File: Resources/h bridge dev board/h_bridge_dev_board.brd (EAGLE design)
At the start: 160 x 100 mm, 99 parts, among them IC1 74LS08N, IC2 74LS08N, IC3 74LS08N, IC4 7404N, IC5 74LS595N, IC6 74158N, IC7 LM358N, J1 J50MM, J2 J50MM, J25 J50MM, J26 J50MM, J27 J50MM, J28 J50MM, J3 J50MM, J4 J50MM

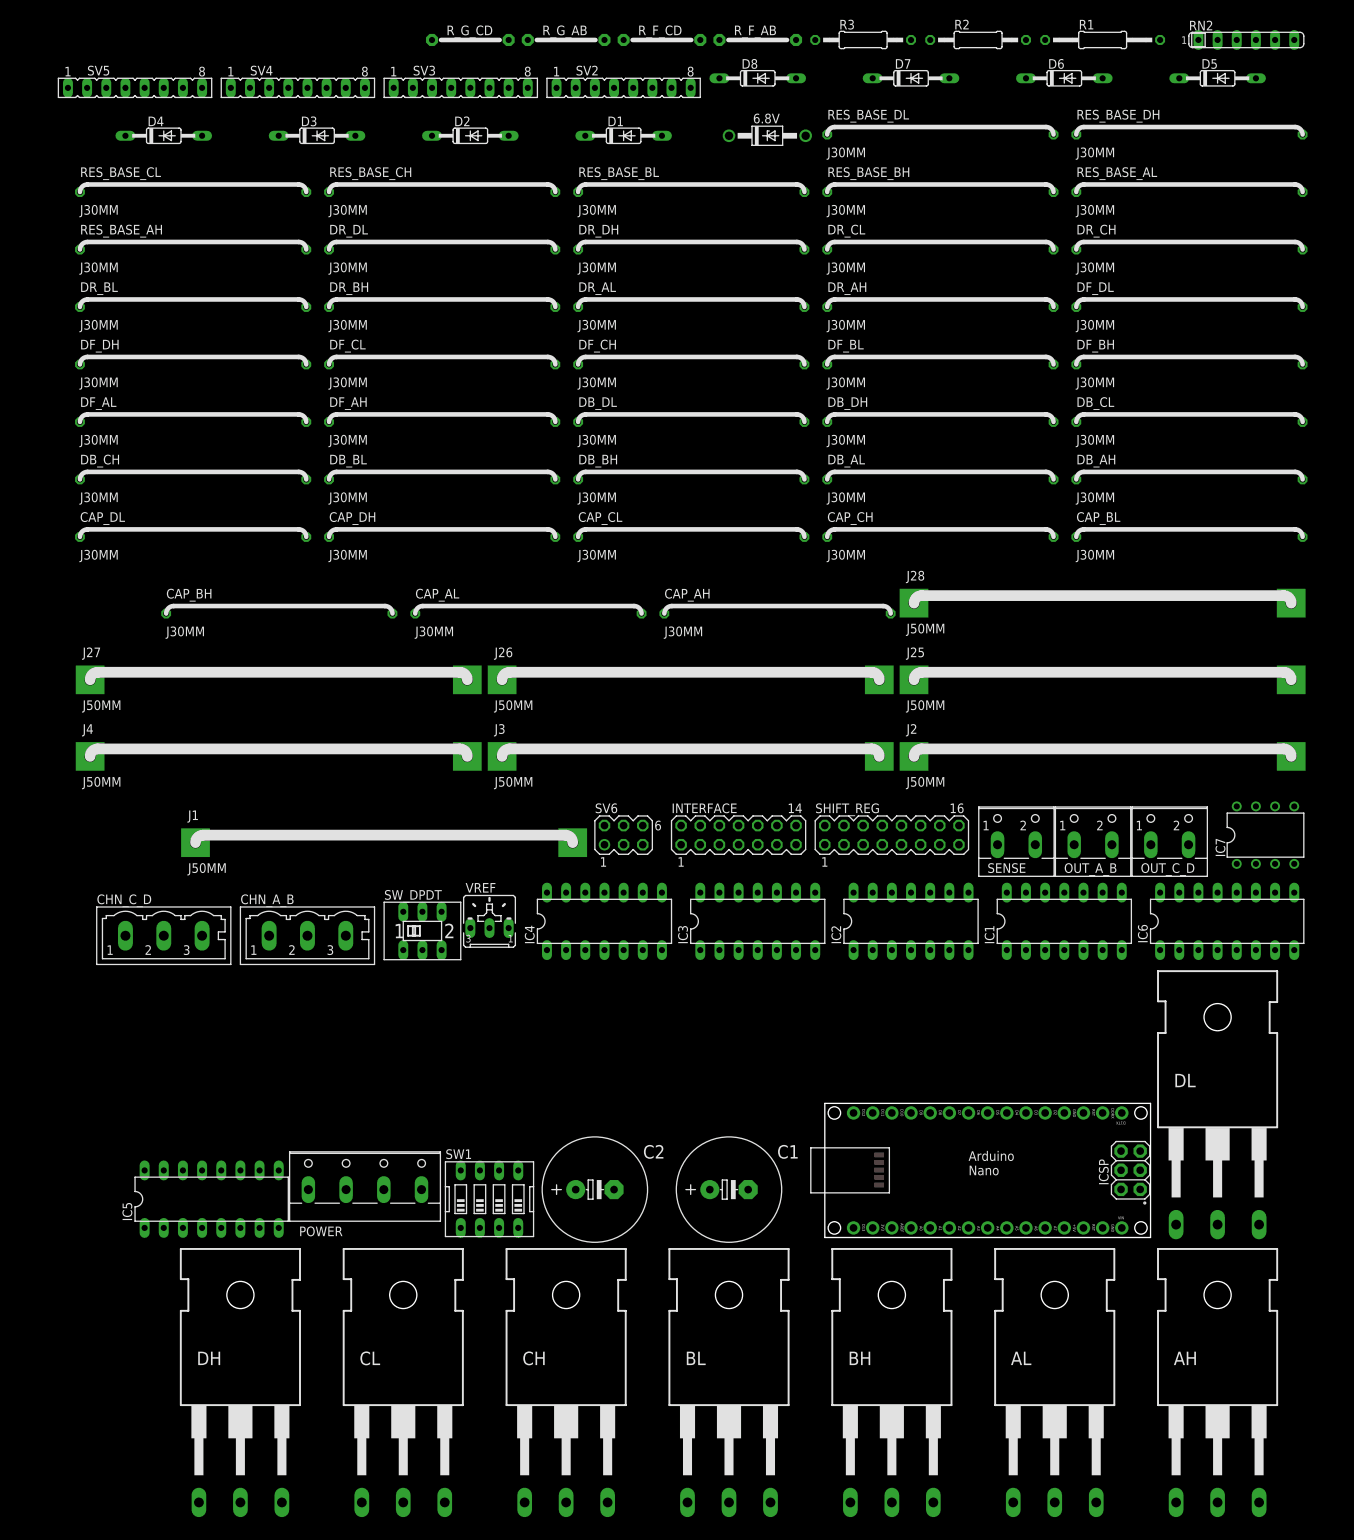
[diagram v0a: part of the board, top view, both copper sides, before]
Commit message: added opto coupler in schematic
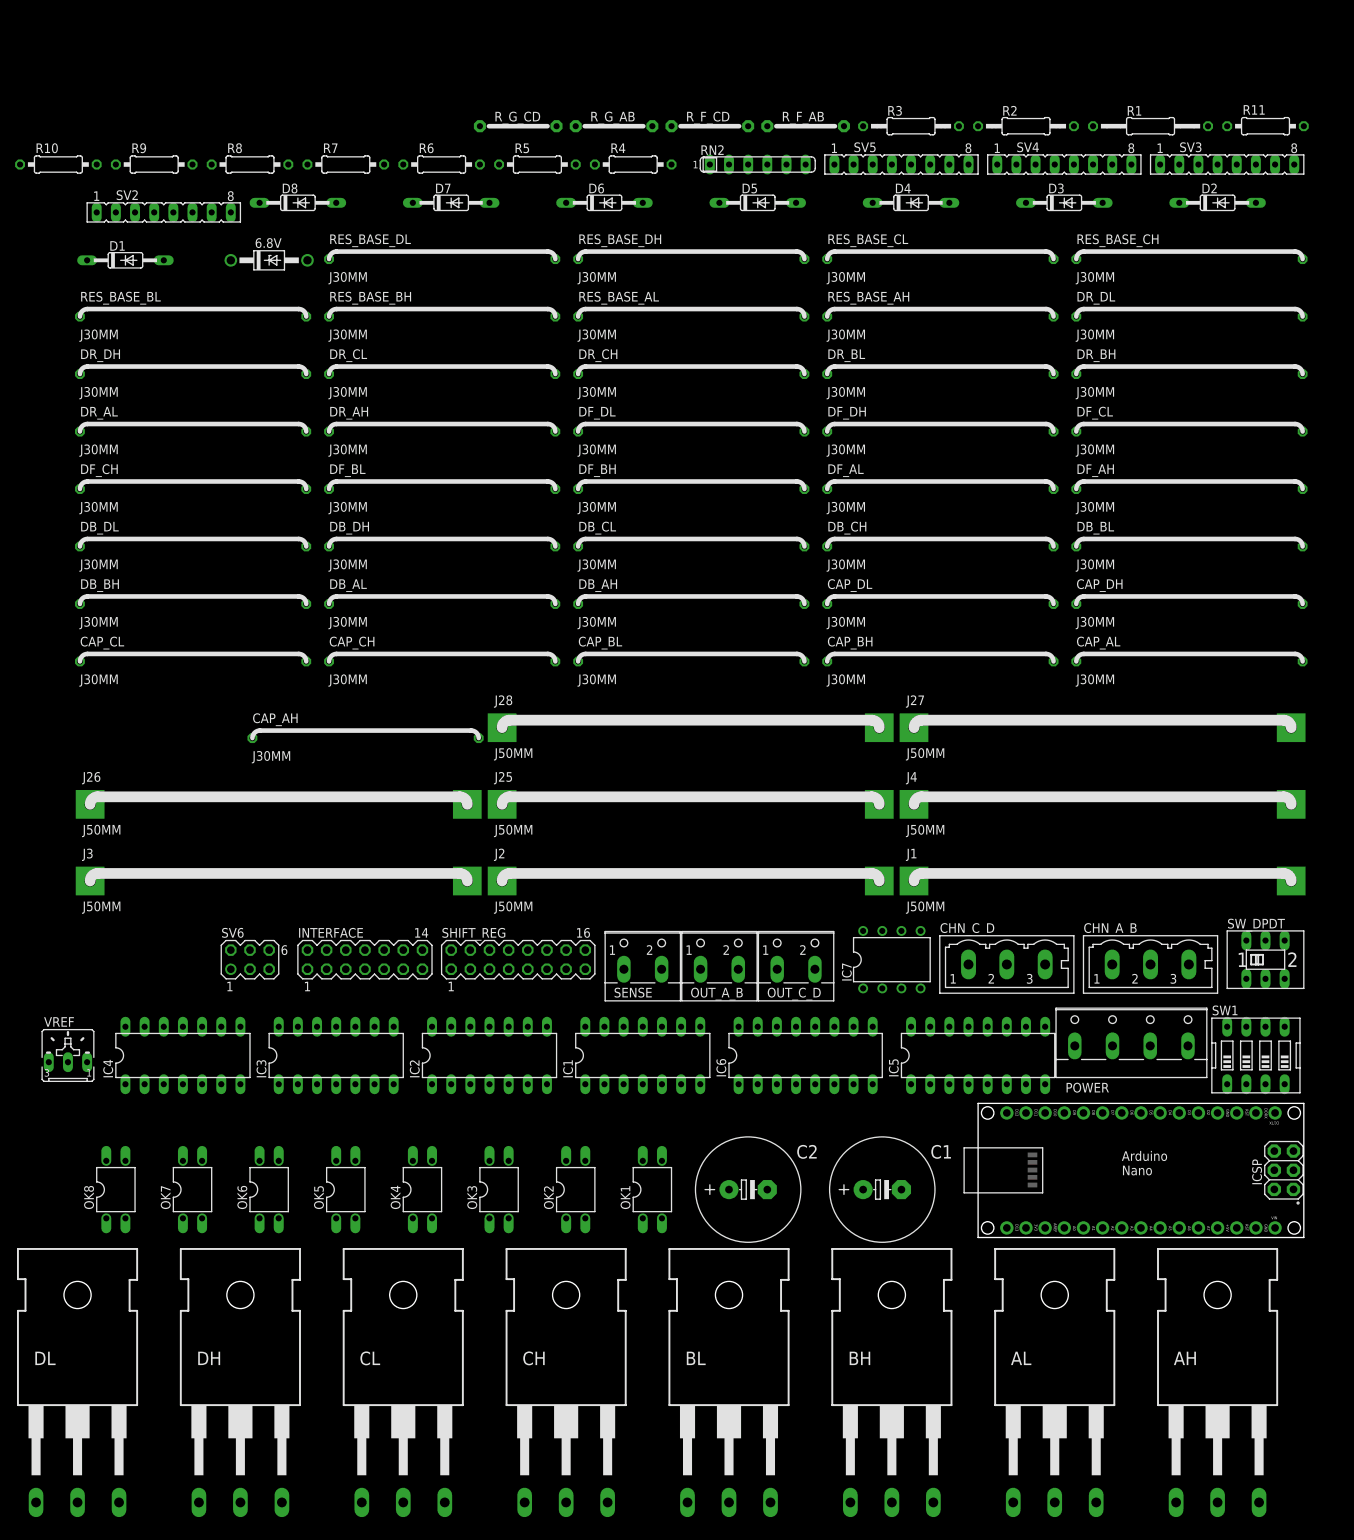
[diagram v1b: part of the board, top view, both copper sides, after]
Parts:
- added OK1, OK2, OK3, OK4, OK5, OK6, OK7, OK8: PC817, optocoupler:DIL04
- added R10, R11, R4, R5, R6, R7, R8, R9: 220, resistor:0207/10
- R2: value 3k -> 3.3k
- moved DL 155.6 mm to (-176.5, 30.5)
- moved CHN_A_B 111.8 mm to (-34.3, 74.9)
- moved SW_DPDT 111.8 mm to (-19.1, 74.9)
- moved CHN_C_D 111.8 mm to (-53.3, 74.9)
- moved J27 109.4 mm to (-40.6, 106.7)
- moved J4 109.4 mm to (-40.6, 96.5)
- moved POWER 103.4 mm to (-36.8, 64.8)
- moved IC5 103.4 mm to (-57.1, 62.2)
- moved SW1 103.4 mm to (-20.3, 62.2)
- moved SV3 102.1 mm to (-24.1, 180.3)
- moved SV4 102.1 mm to (-45.7, 180.3)
- moved SV5 102.1 mm to (-67.3, 180.3)
- moved CAP_DH 99.5 mm to (-29.2, 123.2)
- moved CAP_DL 99.5 mm to (-62.2, 123.2)
- moved D2 99.5 mm to (-25.4, 175.3)
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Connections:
- new net N$12: OK1.1, R4.2
- new net N$14: OK2.1, R5.2
- new net N$15: OK3.1, R6.2
- new net N$17: OK4.1, R7.2
- new net N$27: OK8.1, R11.1
- new net N$30: OK7.1, R10.1
- new net N$32: OK6.1, R9.1
- new net N$33: OK5.1, R8.1
- new net N$34: OK8.3, RES_BASE_DL.2
- new net N$35: OK5.3, RES_BASE_BH.2
- new net N$36: OK6.3, RES_BASE_BL.2
- new net N$37: OK7.3, RES_BASE_DH.2
- new net N$38: OK4.3, RES_BASE_CL.1
- new net N$39: OK3.3, RES_BASE_CH.2
- new net N$42: OK2.3, RES_BASE_AL.1
- new net N$43: OK1.3, RES_BASE_AH.1
- net +5V: now also OK1.4, OK2.4, OK3.4, OK4.4, OK5.4, OK6.4, OK7.4, OK8.4
- net BAKER_CLAMP_AH: now also R4.1; no longer RES_BASE_AH.1
- net BAKER_CLAMP_AL: now also R5.1; no longer RES_BASE_AL.1
- net BAKER_CLAMP_BH: now also R8.2; no longer RES_BASE_BH.2
- net BAKER_CLAMP_BL: now also R9.2; no longer RES_BASE_BL.2
- net BAKER_CLAMP_CH: now also R6.1; no longer RES_BASE_CH.2
- net BAKER_CLAMP_CL: now also R7.1; no longer RES_BASE_CL.1
- net BAKER_CLAMP_DH: now also R10.2; no longer RES_BASE_DH.2
- net BAKER_CLAMP_DL: now also R11.2; no longer RES_BASE_DL.2
- net GND: now also OK1.2, OK2.2, OK3.2, OK4.2, OK5.2, OK6.2, OK7.2, OK8.2

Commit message: reduced jumper size in schematic
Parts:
- removed 6.8V: 1N4738, zener_1n4736A:DO41Z10
- removed R1: 330 ohm 1w, resistor:0207/15
- CAP_AH, CAP_AL, CAP_BH, CAP_BL, CAP_CH, CAP_CL, CAP_DH, CAP_DL, DB_AH, DB_AL, DB_BH, DB_BL, DB_CH, DB_CL, DB_DH, DB_DL, DF_AH, DF_AL, DF_BH, DF_BL, DF_CH, DF_CL, DF_DH, DF_DL, DR_AH, DR_AL, DR_BH, DR_BL, DR_CH, DR_CL, DR_DH, DR_DL, RES_BASE_AH, RES_BASE_AL, RES_BASE_BH, RES_BASE_BL, RES_BASE_CH, RES_BASE_CL, RES_BASE_DH, RES_BASE_DL: value J30MM -> J15MM; device jumper:30 -> jumper:15
- moved DL 393.5 mm to (213.4, 83.8)
- moved CL 346.7 mm to (213.4, 27.9)
- moved DH 318.0 mm to (158.8, 82.5)
- moved CH 271.8 mm to (160.0, 27.9)
- moved BL 201.5 mm to (104.1, 83.8)
- moved AL 149.9 mm to (102.9, 29.2)
- moved BH 135.4 mm to (55.9, 83.8)
- moved AH 81.3 mm to (55.9, 29.2)
- moved C1 29.2 mm to (-71.1, 15.2)
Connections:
- removed net +6.5V: 6.8V.C, IC7.8, R1.2
- net +5V: now also IC7.8
- net GND: no longer 6.8V.A
- net VCC: no longer R1.1
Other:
- board size 160 x 100 mm -> 259.1 x 178.7 mm

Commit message: prili board placement
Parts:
- removed SV6: (no value), con-lstb:MA03-2
- added SENSE_INTERFACE: (no value), con-lstb:MA03-2
- moved J3 355.7 mm to (95.2, -171.4), turned to 180 degrees
- moved J26 341.3 mm to (95.2, -141.0)
- moved J25 317.5 mm to (95.2, -157.5), turned to 180 degrees
- moved DH 313.4 mm to (-63.5, -138.4)
- moved DL 309.1 mm to (26.7, -162.6), turned to 270 degrees
- moved D8 293.1 mm to (-101.6, -114.3)
- moved D6 289.8 mm to (-119.4, -114.3)
- moved D5 283.9 mm to (-119.4, -106.7)
- moved D7 283.1 mm to (-101.6, -106.7)
- moved INTERFACE 277.7 mm to (97.8, 221.0), turned to 180 degrees
- moved OUT_A_B 268.0 mm to (124.5, -83.8), turned to 90 degrees
- moved J4 259.4 mm to (95.2, -124.5)
- moved OUT_C_D 253.8 mm to (124.5, -73.7), turned to 90 degrees
- moved CH 247.7 mm to (-63.5, -78.7)
- moved J28 235.8 mm to (88.9, -40.6)
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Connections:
- net A0: now also SENSE_INTERFACE.2; no longer SV6.6
- net A1: now also SENSE_INTERFACE.4; no longer SV6.4
- net A2: now also SENSE_INTERFACE.6; no longer SV6.2
- net SENSE01: now also SENSE_INTERFACE.1; no longer SV6.5
- net SENSE02: now also SENSE_INTERFACE.3; no longer SV6.3
- net VREF: now also SENSE_INTERFACE.5; no longer SV6.1
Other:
- board size 259.1 x 178.7 mm -> 261.6 x 435.6 mm

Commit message: microstep works with l298 at 20KHz. ipdate schematic with active RC low pass filters
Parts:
- added C3, C4: 100n, rcl:C050-030X075
- added IC8: LM358N, linear:DIL08
- added R1, R12: 2.2k, rcl:0207/10
- CAP_AH, CAP_AL, CAP_BH, CAP_BL, CAP_CH, CAP_CL, CAP_DH: value J15MM -> (none); device jumper:15 -> rcl:C050-030X075
- CAP_DL: device jumper:15 -> rcl:C050-030X075
- DB_AH, DB_AL, DB_BH, DB_BL, DB_CH, DB_CL, DB_DH, DB_DL, DF_AH, DF_AL, DF_BH, DF_BL, DF_CH, DF_CL, DF_DH, DF_DL, DR_AH, DR_AL, DR_BH, DR_BL, DR_CH, DR_CL, DR_DH, DR_DL: value J15MM -> (none); device jumper:15 -> diode:DO27-15
- R10, R11, R4, R5, R6, R7, R8, R9: device resistor:0207/10 -> rcl:0207/10
- R2, R3: device resistor:0207/12 -> rcl:0207/10
- RES_BASE_AH, RES_BASE_AL, RES_BASE_BH, RES_BASE_BL, RES_BASE_CH, RES_BASE_CL, RES_BASE_DH: value J15MM -> (none); device jumper:15 -> rcl:0207/10
- RES_BASE_DL: device jumper:15 -> rcl:0207/10
- R_F_AB, R_F_CD, R_G_AB, R_G_CD: value J10MM -> (none); device jumper:10 -> rcl:0207/10
- moved DR_DL 487.5 mm to (-121.9, -397.5)
- moved DB_DL 476.9 mm to (-121.9, -389.9)
- moved DF_DL 476.9 mm to (-121.9, -382.3)
- moved DR_DH 454.3 mm to (-121.9, -374.6)
- moved DB_DH 450.7 mm to (-121.9, -367.0)
- moved DF_DH 447.1 mm to (-121.9, -359.4)
- moved DB_BL 425.8 mm to (-121.9, -344.2)
- moved DR_BL 425.8 mm to (-121.9, -351.8)
- moved DF_BL 414.9 mm to (-121.9, -336.6)
- moved DB_BH 398.1 mm to (-121.9, -321.3)
- moved DR_BH 398.1 mm to (-121.9, -328.9)
- moved DF_BH 387.1 mm to (-121.9, -313.7)
- moved DF_AH 362.2 mm to (-121.9, -306.1)
- moved DB_AH 358.4 mm to (-121.9, -298.4)
- moved DR_AH 343.1 mm to (-121.9, -290.8)
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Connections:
- removed net N$10: CAP_AL.1, RES_BASE_AL.2
- removed net N$22: CAP_CH.1, RES_BASE_CH.1
- removed net N$23: CAP_CL.1, RES_BASE_CL.2
- removed net N$24: CAP_BH.2, RES_BASE_BH.1
- removed net N$26: CAP_BL.2, RES_BASE_BL.1
- removed net N$28: CAP_DH.2, RES_BASE_DH.1
- removed net N$7: CAP_DL.1, DB_DL.1, DF_DL.1, DR_DL.1
- removed net N$9: CAP_AH.1, RES_BASE_AH.2
- new net N$46: C3.1, IC8.5, R1.1
- new net N$47: C4.1, IC8.3, R12.1
- new net SENSE01_FILTER: IC8.6, IC8.7, SENSE_INTERFACE.1
- new net SENSE02_FILTER: IC8.1, IC8.2, SENSE_INTERFACE.3
- net +5V: now also IC8.8
- net AH: now also DB_AH.C, DR_AH.A; no longer DB_AH.2, DR_AH.2
- net AL: now also DB_AL.C, DR_AL.A; no longer DB_AL.2, DR_AL.2
- net BH: now also DB_BH.C, DR_BH.A; no longer DB_BH.2, DR_BH.2
- net BL: now also DB_BL.C, DR_BL.A; no longer DB_BL.2, DR_BL.2
- net CH: now also DB_CH.C, DR_CH.A; no longer DB_CH.2, DR_CH.2
- net CL: now also DB_CL.C, DR_CL.A; no longer DB_CL.2, DR_CL.2
- net DH: now also DB_DH.C, DR_DH.A; no longer DB_DH.2, DR_DH.2
- net DL: now also DB_DL.C, DR_DL.A; no longer DB_DL.2, DR_DL.2
- net GND: now also C3.2, C4.2, IC8.4
- net N$19: now also DB_CL.A, DF_CL.A, DR_CL.C, RES_BASE_CL.2; no longer DB_CL.1, DF_CL.1, DR_CL.1
- net N$20: now also DB_AH.A, DF_AH.A, DR_AH.C, RES_BASE_AH.2; no longer DB_AH.1, DF_AH.1, DR_AH.1
- net N$21: now also DB_BH.A, DF_BH.A, DR_BH.C, RES_BASE_BH.1; no longer DB_BH.1, DF_BH.1, DR_BH.1
- net N$29: now also CAP_DL.1, DB_DL.A, DF_DL.A, DR_DL.C; no longer CAP_DL.2
- net N$34: now also CAP_DL.2
- net N$35: now also CAP_BH.2
- net N$36: now also CAP_BL.2
- net N$37: now also CAP_DH.2
- net N$38: now also CAP_CL.1
- net N$39: now also CAP_CH.1
- net N$4: now also DB_AL.A, DF_AL.A, DR_AL.C, RES_BASE_AL.2; no longer DB_AL.1, DF_AL.1, DR_AL.1
- net N$42: now also CAP_AL.1
- net N$43: now also CAP_AH.1
- net N$5: now also DB_CH.A, DF_CH.A, DR_CH.C, RES_BASE_CH.1; no longer DB_CH.1, DF_CH.1, DR_CH.1
- net N$6: now also DB_BL.A, DF_BL.A, DR_BL.C, RES_BASE_BL.1; no longer DB_BL.1, DF_BL.1, DR_BL.1
- net N$8: now also DB_DH.A, DF_DH.A, DR_DH.C, RES_BASE_DH.1; no longer DB_DH.1, DF_DH.1, DR_DH.1
- net OUT_A: now also DF_AL.C; no longer DF_AL.2
- net OUT_B: now also DF_BL.C; no longer DF_BL.2
- net OUT_C: now also DF_CL.C; no longer DF_CL.2
- net OUT_D: now also DF_DL.C; no longer DF_DL.2
- net SENSE01: now also R1.2; no longer SENSE_INTERFACE.1
- net SENSE02: now also R12.2; no longer SENSE_INTERFACE.3
- net VCC: now also DF_AH.C, DF_BH.C, DF_CH.C, DF_DH.C; no longer DF_AH.2, DF_BH.2, DF_CH.2, DF_DH.2
